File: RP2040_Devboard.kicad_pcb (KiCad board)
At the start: 2 copper layers, 42.2 x 64 mm, 39 parts, among them J1 USB_B_Mini, J2 Conn_01x03_Socket, J3 Conn_01x22, J5 Conn_01x22, SW1 SW_Push, SW2 SW_Push, U1 RP2040, U2 AP2112K-1.2, U3 USBLC6-2SC6, U4 W25Q128JVS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

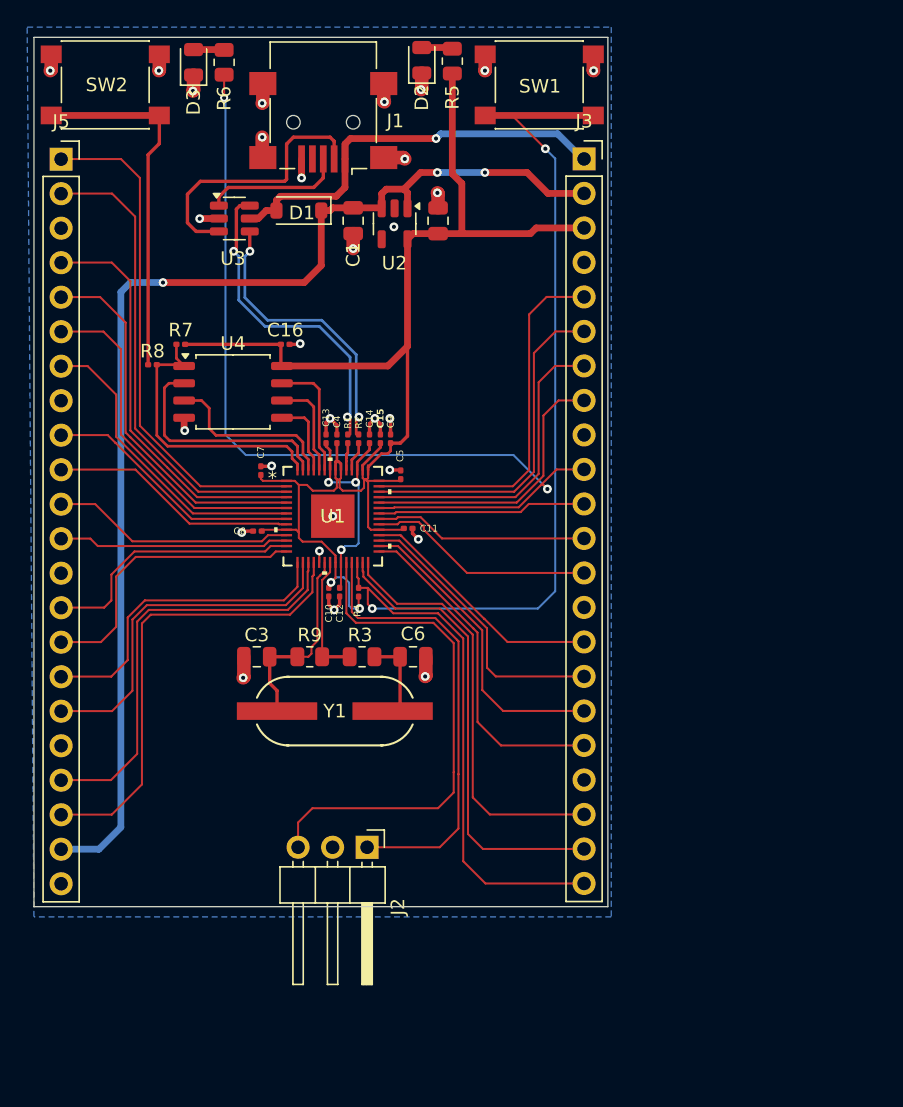
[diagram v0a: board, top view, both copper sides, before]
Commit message: Added gnd zone on top layer
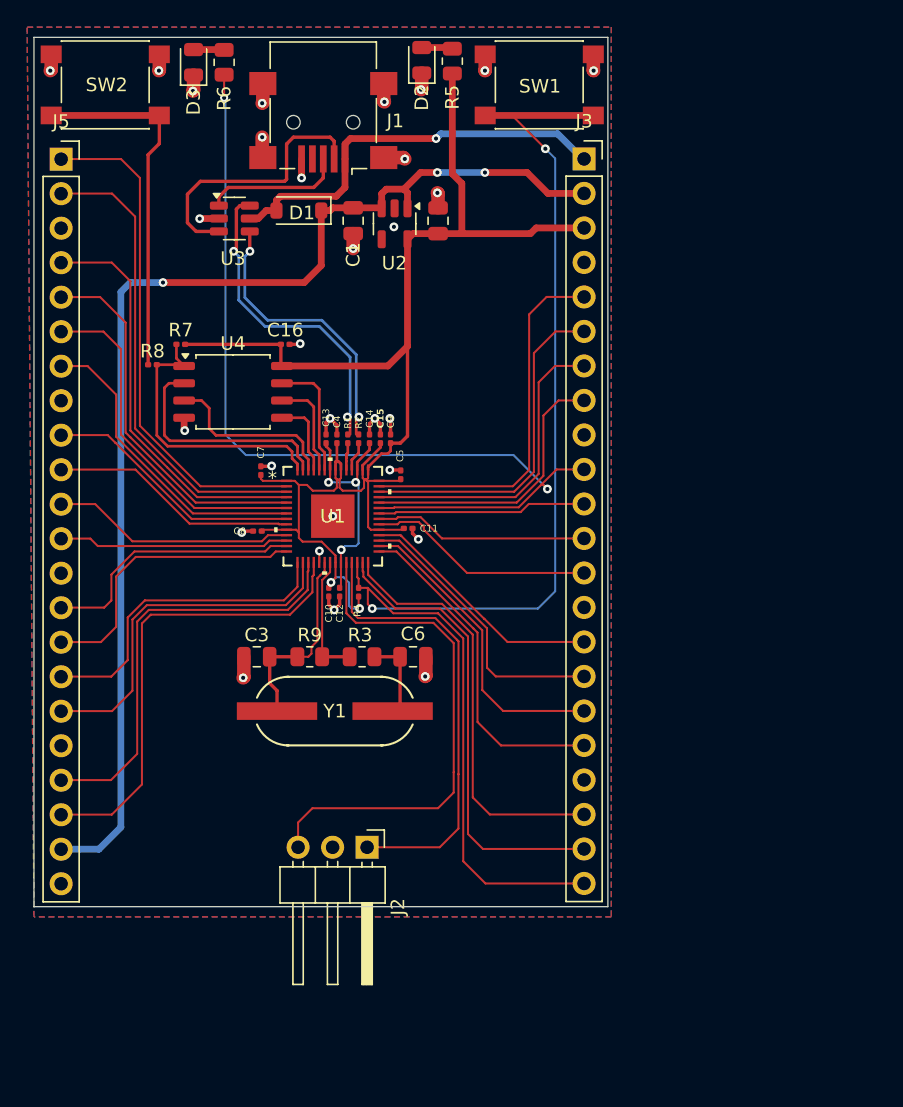
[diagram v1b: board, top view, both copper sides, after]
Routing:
- added copper zone on F.Cu, net GND
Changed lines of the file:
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@@
+		(net 16)
+		(net_name "GND")
+		(layer "F.Cu")
+		(hatch edge 0.5)
+		(priority 1)
+		(connect_pads
+			(clearance 0.3)
+		)
+		(min_thickness 0.25)
+		(filled_areas_thickness no)
+		(fill yes
+			(thermal_gap 0.5)
+			(thermal_bridge_width 0.5)
+		)
+		(polygon
+			(pts
+				(xy 103.5 59.5) (xy 146.5 59.5) (xy 146.5 125) (xy 104 125)
+			)
+		)
+	)
+	(zone
 		(net 16)
 		(net_name "GND")

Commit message: Some lauayt changes
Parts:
- moved C10 0.81 mm to (125.7, 101.9)
- moved C12 0.81 mm to (126.5, 101.9)
- moved R4 0.30 mm to (128.2, 101.1)
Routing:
- net +3.3V: track 108.5 -> 125.8 mm, vias 2 -> 3
- net /RUN: track 99.1 -> 113.8 mm, vias 2 -> 1
- net /XIN: track 16.6 -> 14.0 mm
- net GND: track 36.3 -> 34.0 mm, vias 29 -> 28
- net +1V1: track 17.3 -> 18.1 mm

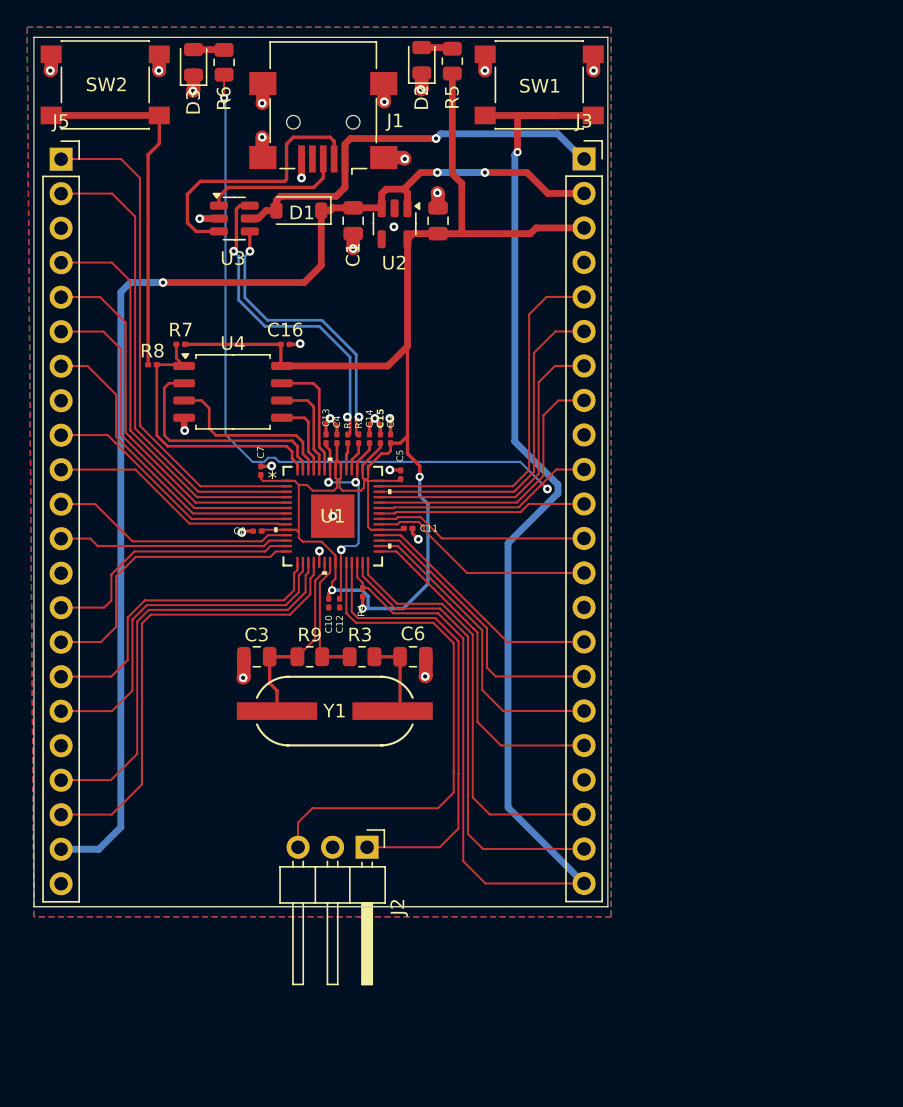
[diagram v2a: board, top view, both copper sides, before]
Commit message: Added RC for each button, deleted extra pins
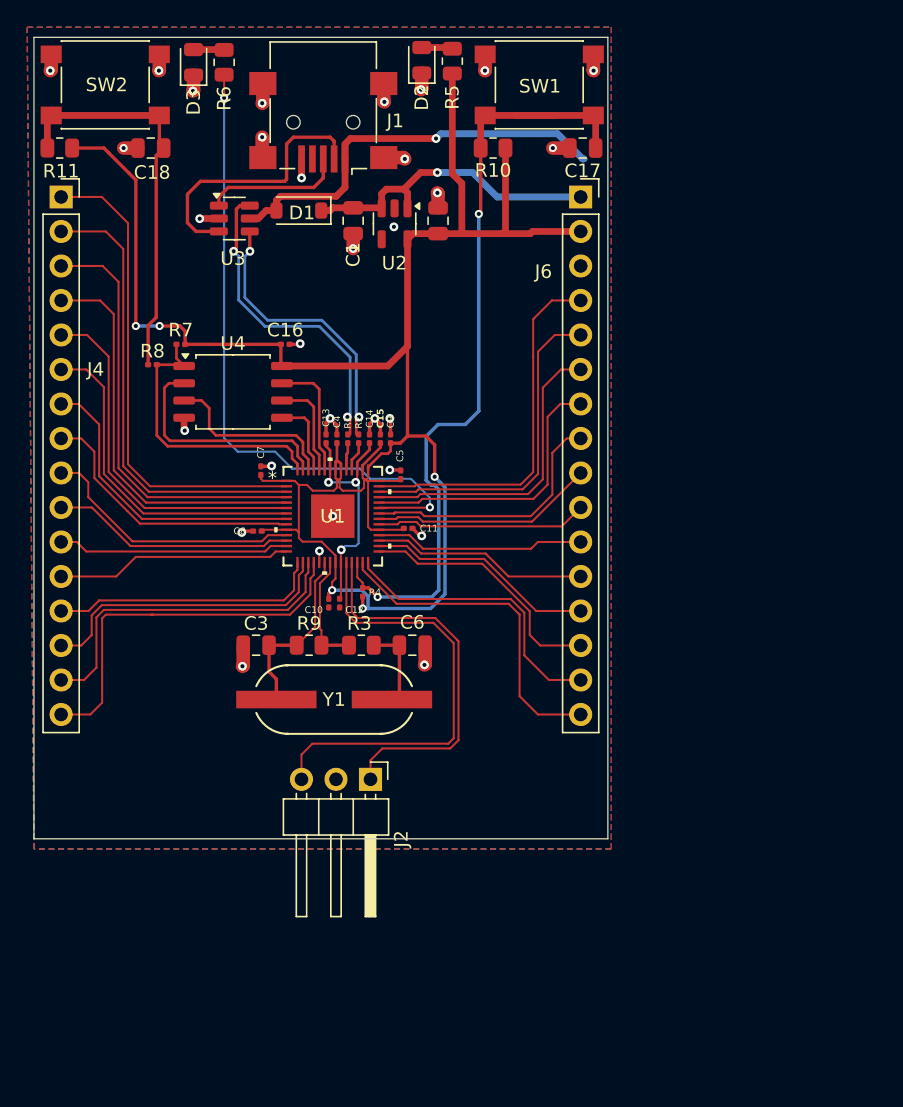
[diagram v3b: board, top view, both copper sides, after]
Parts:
- removed J3, J5: Conn_01x22, Connector_PinSocket_2.54mm:PinSocket_1x22_P2.54mm_Vertical
- added C17: 1uF, Capacitor_SMD:C_0805_2012Metric, F.Cu at (144.4, 68.4)
- added C18: 1uF, Capacitor_SMD:C_0805_2012Metric, F.Cu at (112.6, 68.4)
- added J4: Conn_01x16, Connector_PinSocket_2.54mm:PinSocket_1x16_P2.54mm_Vertical, F.Cu at (106.0, 72.0)
- added J6: Conn_01x16, Connector_PinSocket_2.54mm:PinSocket_1x16_P2.54mm_Vertical, F.Cu at (144.2, 72.0)
- added R10: 10k, Resistor_SMD:R_0805_2012Metric, F.Cu at (137.8, 68.4)
- added R11: 10k, Resistor_SMD:R_0805_2012Metric, F.Cu at (105.9, 68.4)
- moved J2 5.01 mm to (128.8, 114.9)
- moved C6 0.85 mm to (131.9, 105.0)
- moved R3 0.85 mm to (128.1, 105.0)
- moved R9 0.85 mm to (124.3, 105.0)
- moved Y1 0.85 mm to (126.1, 109.0)
- moved C3 0.85 mm to (120.4, 105.0)
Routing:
- net /VSYS: track 87.4 -> 23.2 mm, vias 3 -> 1
- net /RUN: track 113.8 -> 64.1 mm, vias 1 -> 2
- net +3.3V: track 125.8 -> 156.0 mm, vias 3 -> 5
- net /GPIO25: track 69.0 -> 48.9 mm
- net /GPIO17: track 31.1 -> 21.3 mm
- net /GPIO16: track 34.1 -> 24.5 mm
- net /GPIO14: track 31.7 -> 25.1 mm
- net /GPIO15: track 34.5 -> 28.3 mm
- net /GPIO18: track 24.9 -> 18.7 mm
- net /GPIO19: track 22.7 -> 16.8 mm
- net /SWDIO: track 33.5 -> 28.2 mm
- net /GPIO20: track 20.9 -> 15.9 mm
- net /SWCLK: track 37.7 -> 33.1 mm
- net /GPIO13: track 26.5 -> 22.3 mm
- net /GPIO11: track 21.5 -> 17.4 mm
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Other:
- board size 42.2 x 64 mm -> 42.2 x 59 mm

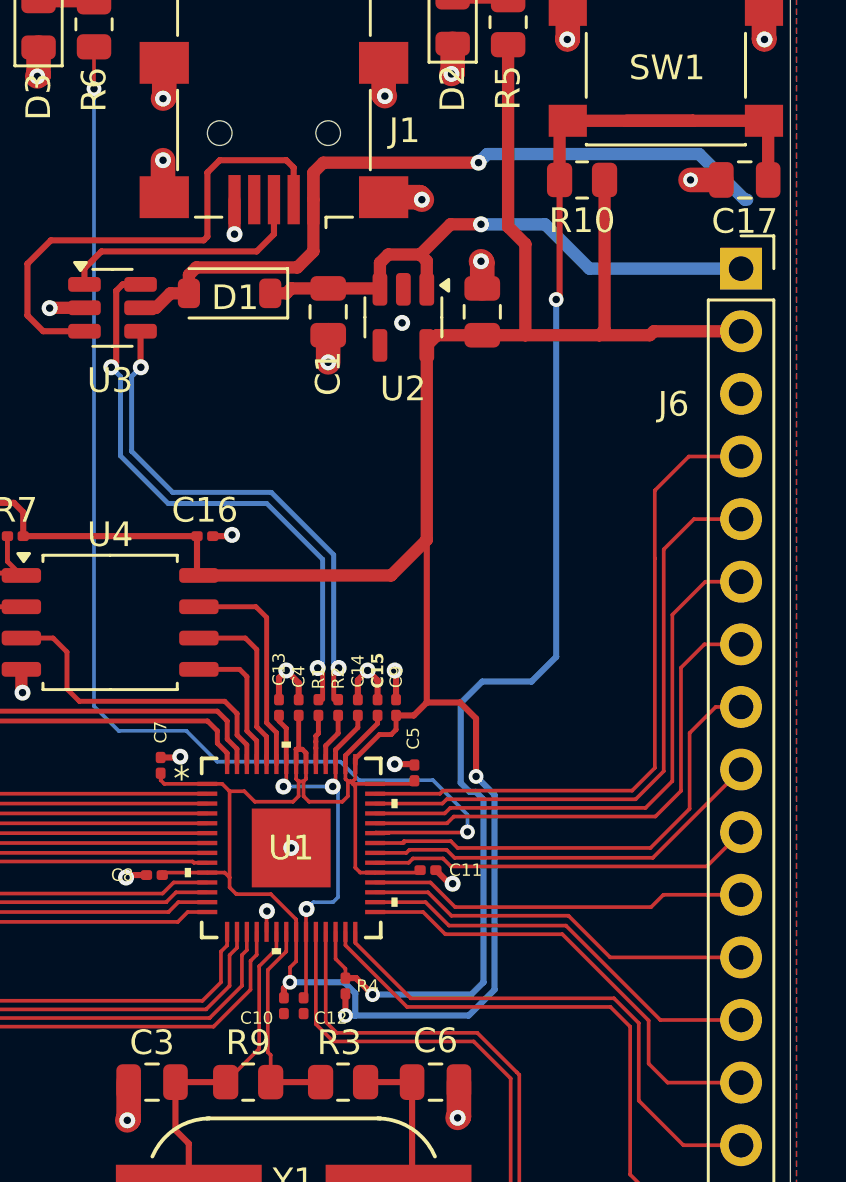
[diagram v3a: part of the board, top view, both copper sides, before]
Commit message: Better vias
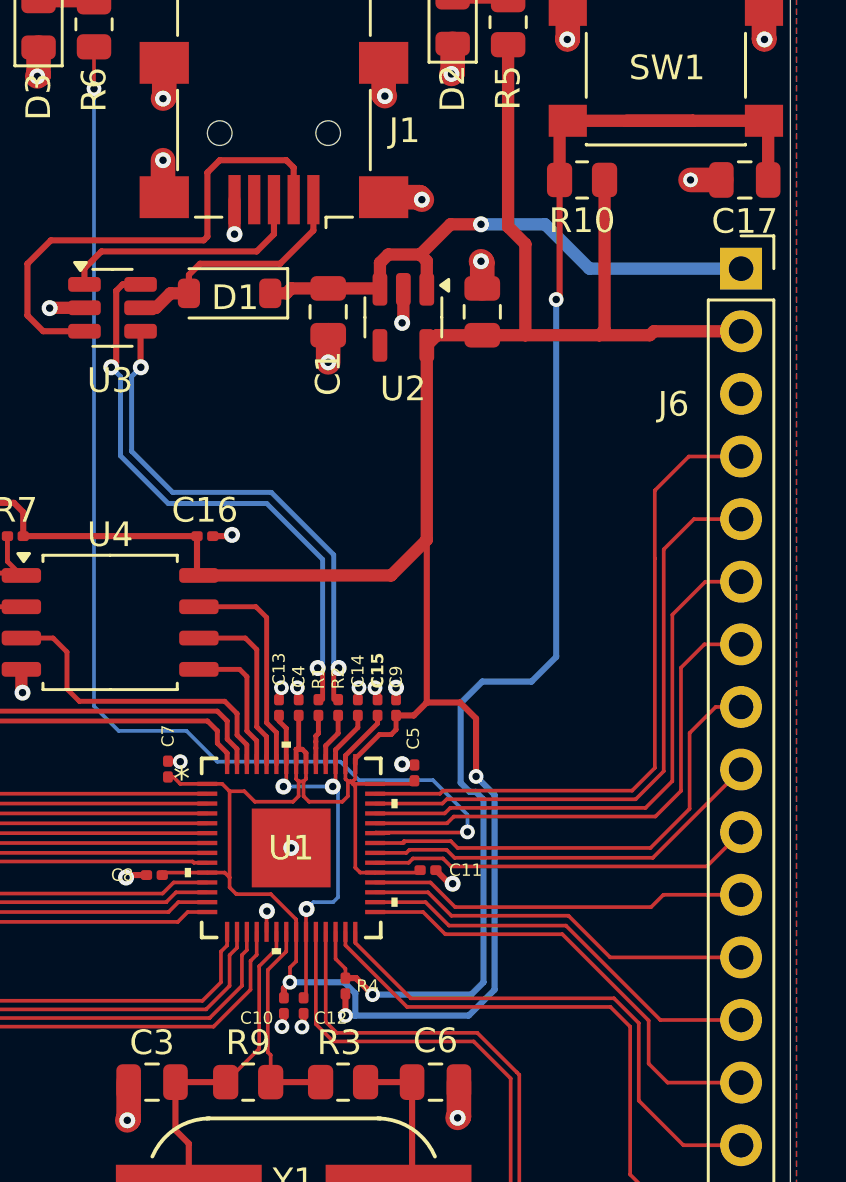
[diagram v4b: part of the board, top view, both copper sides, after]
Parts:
- moved C7 0.33 mm to (121.0, 92.3)
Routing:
- net /VBUS: track 30.3 -> 10.0 mm, vias 1 -> 0
- net GND: track 36.3 -> 34.1 mm, vias 30 -> 34
- net +3.3V: track 156.0 -> 155.4 mm

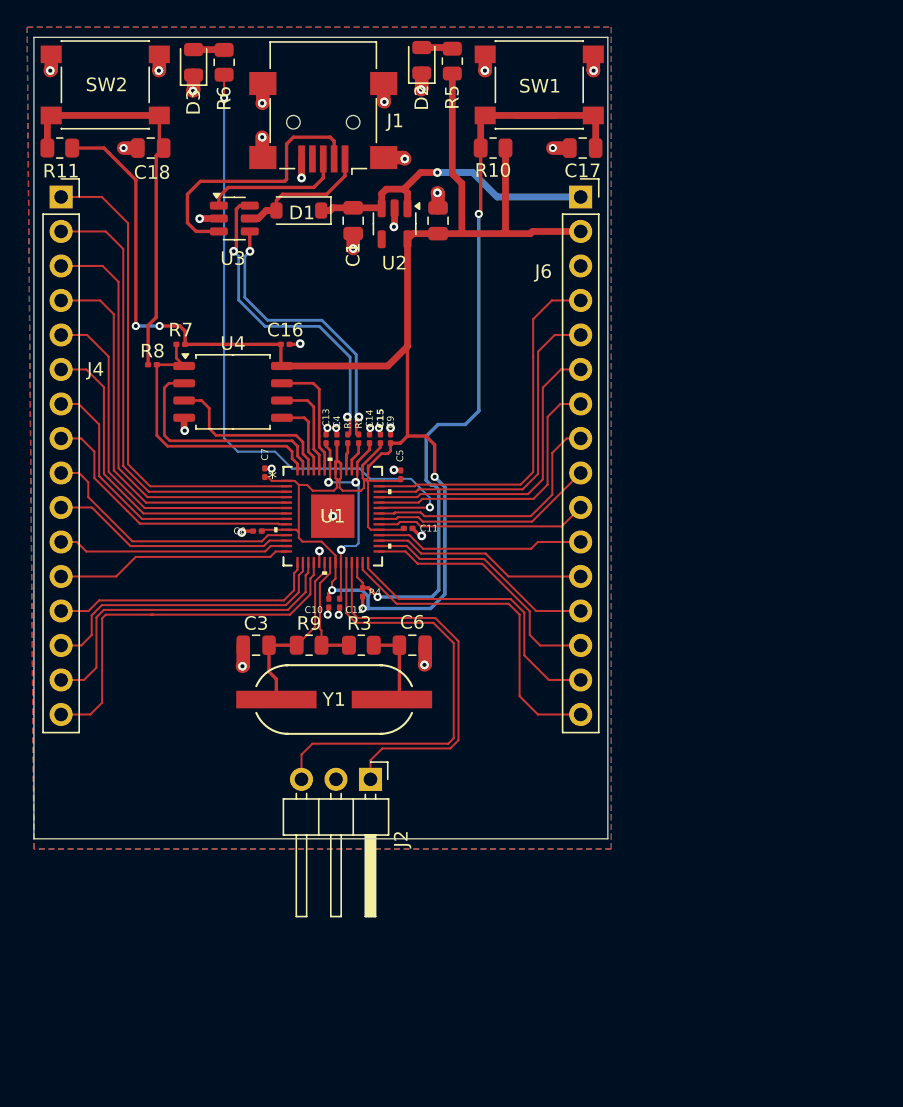
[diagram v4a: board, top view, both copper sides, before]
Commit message: Added mointing holes and stetching vias
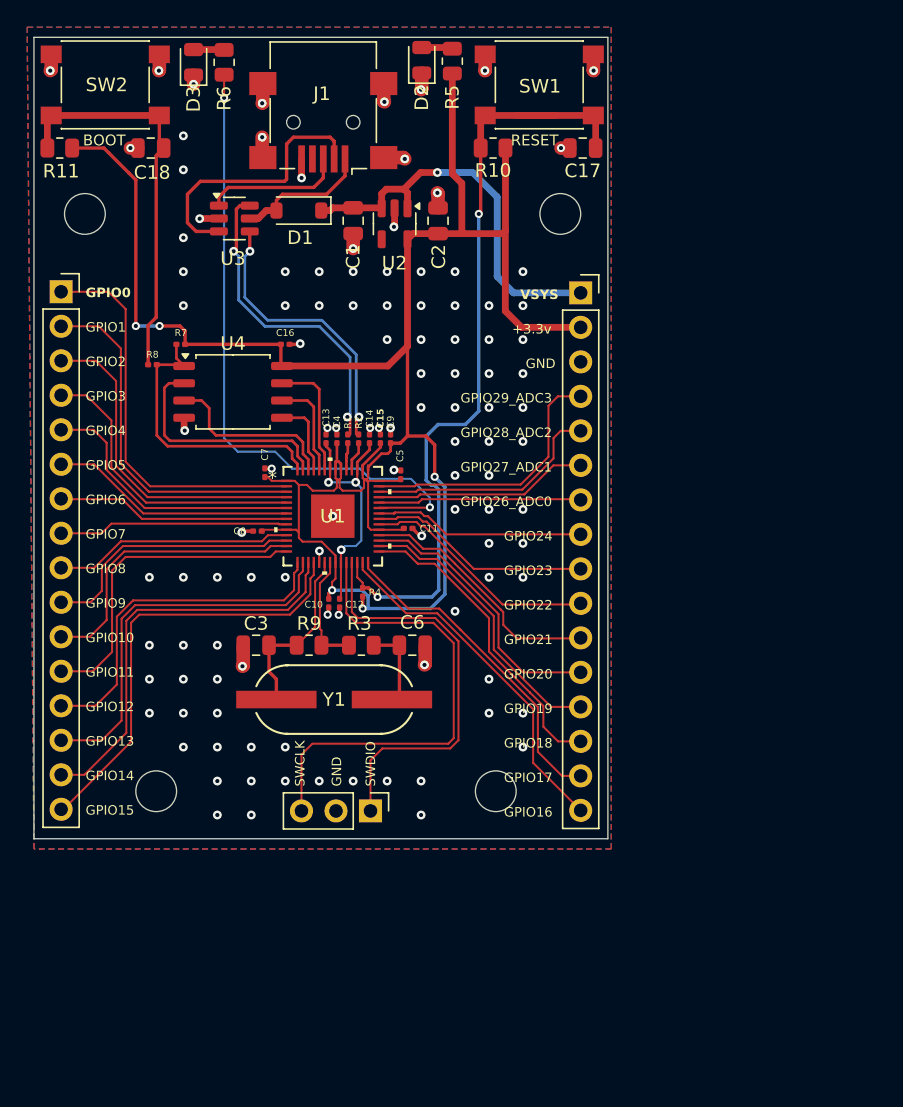
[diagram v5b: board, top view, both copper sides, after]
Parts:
- added H1: MountingHole, MountingHole:MountingHole_3mm, F.Cu at (142.8, 73.2)
- added H2: MountingHole, MountingHole:MountingHole_3mm, F.Cu at (107.8, 73.2)
- added H3: MountingHole, MountingHole:MountingHole_3mm, F.Cu at (138.0, 115.8)
- added H4: MountingHole, MountingHole:MountingHole_3mm, F.Cu at (113.0, 115.8)
- J2: footprint Connector_PinHeader_2.54mm:PinHeader_1x03_P2.54mm_Horizontal -> Connector_PinHeader_2.54mm:PinHeader_1x03_P2.54mm_Vertical
- moved J6 7.06 mm to (144.2, 79.1)
- moved J4 6.98 mm to (106.0, 79.0)
- moved J2 2.33 mm to (128.8, 117.2)
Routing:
- net /GPIO3: track 29.5 -> 21.9 mm
- net /GPIO29_ADC3: track 27.1 -> 19.8 mm
- net /GPIO28_ADC2: track 24.9 -> 17.6 mm
- net /GPIO1: track 33.9 -> 26.6 mm
- net /GPIO2: track 31.7 -> 24.4 mm
- net /GPIO27_ADC1: track 22.7 -> 15.8 mm
- net /GPIO4: track 26.9 -> 20.2 mm
- net /GPIO0: track 35.8 -> 29.1 mm
- net /GPIO5: track 24.7 -> 18.1 mm
- net /GPIO13: track 22.3 -> 28.7 mm
- net /GPIO11: track 17.4 -> 23.8 mm
- net /VSYS: track 23.2 -> 29.5 mm
- net +3.3V: track 155.4 -> 161.6 mm
- net /GPIO12: track 19.9 -> 25.8 mm
- net /GPIO26_ADC0: track 20.8 -> 15.0 mm
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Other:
- board text added: "+3.3v"
- board text added: "BOOT"
- board text added: "GND"
- board text added: "GPIO0"
- board text added: "GPIO1"
- board text added: "GPIO10"
- board text added: "GPIO11"
- board text added: "GPIO12"
- board text added: "GPIO13"
- board text added: "GPIO14"
- board text added: "GPIO15"
- board text added: "GPIO16"
- board text added: "GPIO17"
- board text added: "GPIO18"
- board text added: "GPIO19"
- board text added: "GPIO2"
- board text added: "GPIO20"
- board text added: "GPIO21"
- board text added: "GPIO22"
- board text added: "GPIO23"
- board text added: "GPIO24"
- board text added: "GPIO26_ADC0"
- board text added: "GPIO27_ADC1"
- board text added: "GPIO28_ADC2"
- board text added: "GPIO29_ADC3"
- board text added: "GPIO3"
- board text added: "GPIO4"
- board text added: "GPIO5"
- board text added: "GPIO6"
- board text added: "GPIO7"
- board text added: "GPIO8"
- board text added: "GPIO9"
- board text added: "RESET"
- board text added: "SWCLK"
- board text added: "SWDIO"
- board text added: "VSYS"
